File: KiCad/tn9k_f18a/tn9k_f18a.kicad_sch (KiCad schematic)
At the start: 9 parts, among them J1 Conn_01x20, J2 Conn_01x20, J3 Conn_01x24, J4 Conn_01x24, J5 Conn_02x04_Counter_Clockwise, J6 Conn_02x08_Odd_Even, U1 SN74LVC245, U2 SN74LVC245, U3 SN74LVC245

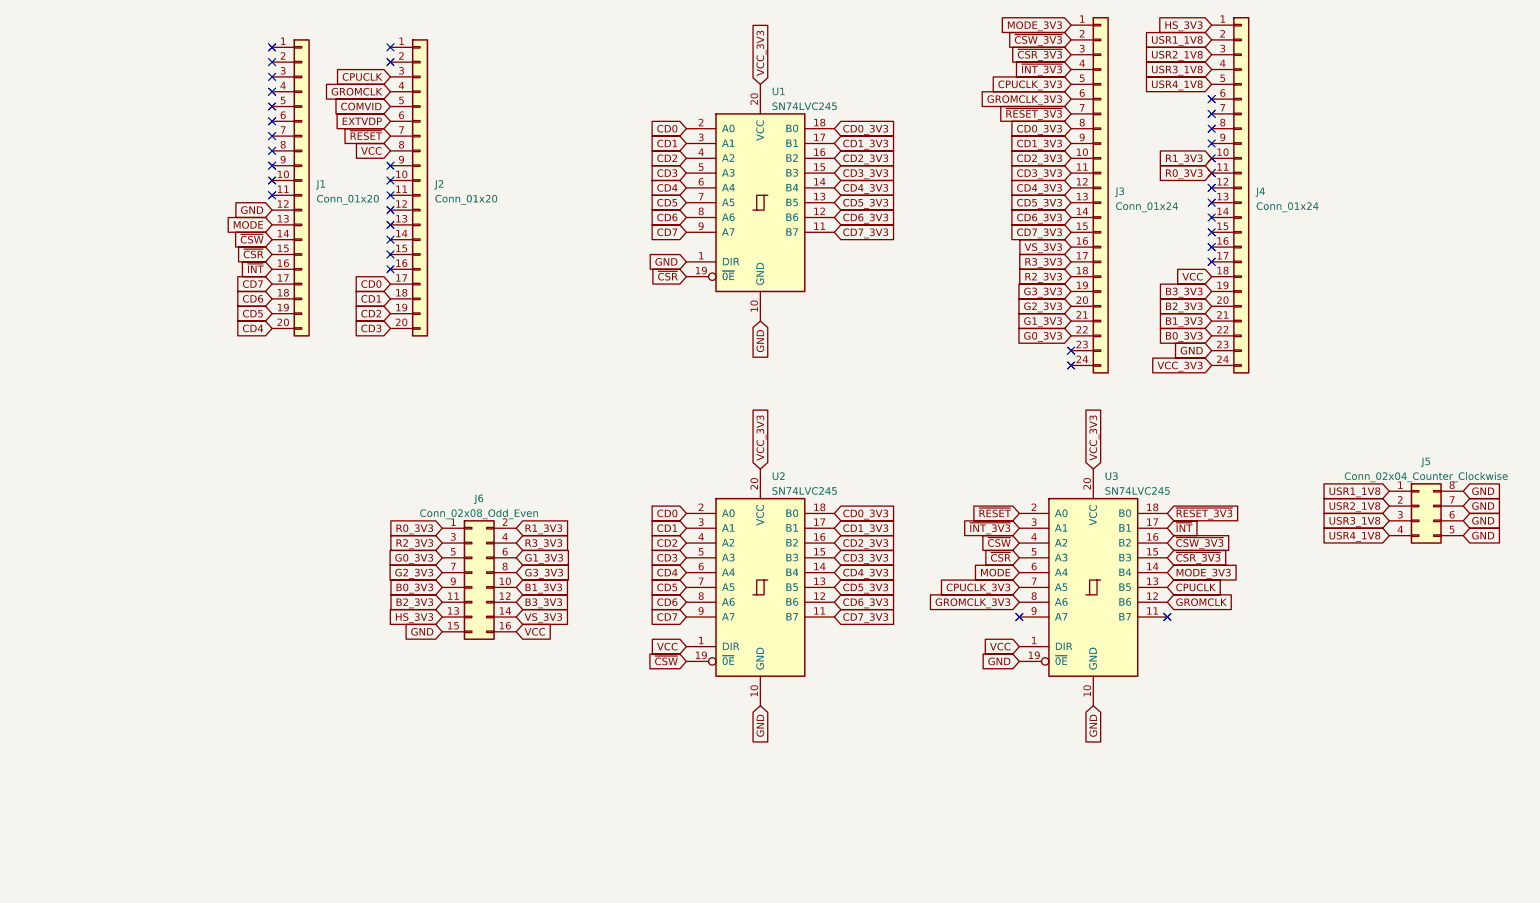
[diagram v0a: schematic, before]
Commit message: SMD version
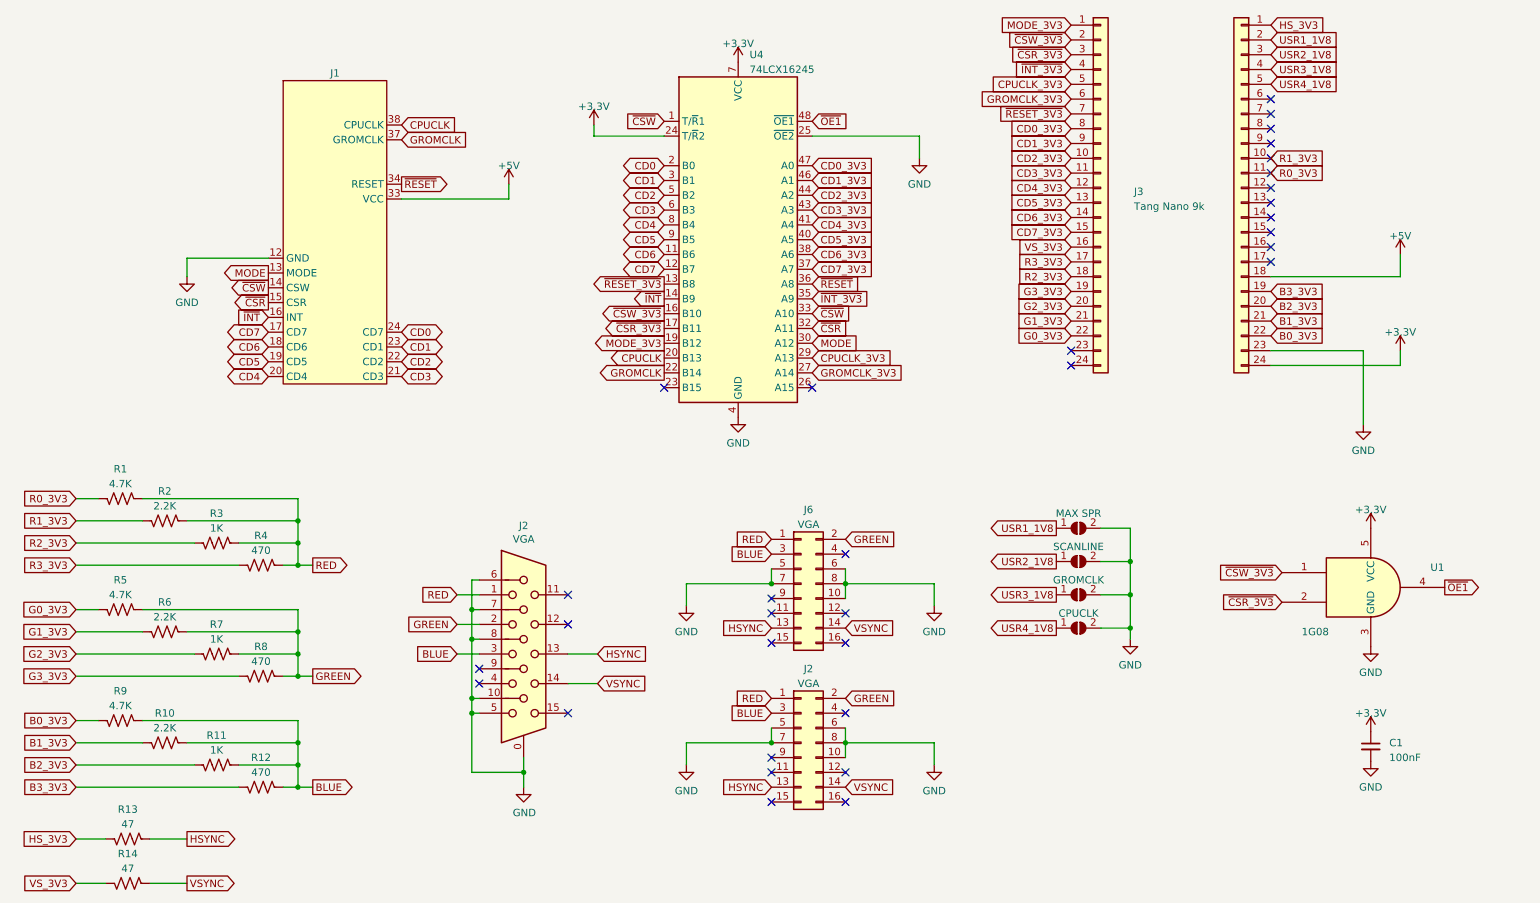
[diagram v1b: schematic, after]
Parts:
- removed J1, J2: Conn_01x20, Connector_PinHeader_2.54mm:PinHeader_1x20_P2.54mm_Vertical, symbol Connector_Generic:Conn_01x20
- removed J5: Conn_02x04_Counter_Clockwise, Button_Switch_THT:SW_DIP_SPSTx04_Slide_6.7x11.72mm_W7.62mm_P2.54mm_LowProfile, symbol Connector_Generic:Conn_02x04_Counter_Clockwise
- removed U1, U2, U3: SN74LVC245, Package_DIP:DIP-20_W7.62mm_Socket_LongPads, symbol tms9118a_sym:SN74LVC245
- added C1: 100nF, Capacitor_SMD:C_0603_1608Metric_Pad1.08x0.95mm_HandSolder, symbol Device:C_Small
- added J1: ~, f18a_footprints:TMS99xxA_Replacement, symbol f18a_tn9k:TMS99xxA_Replacement
- added J2: VGA, Connector_Dsub:DSUB-15-HD_Female_Horizontal_P2.29x1.98mm_EdgePinOffset3.03mm_Housed_MountingHolesOffset4.94mm, symbol Connector:DB15_Female_HighDensity_MountingHoles
- added J2: VGA, Connector_PinHeader_2.54mm:PinHeader_2x08_P2.54mm_Vertical, symbol Connector_Generic:Conn_02x08_Odd_Even
- added JP1: MAX SPR, Jumper:SolderJumper-2_P1.3mm_Open_RoundedPad1.0x1.5mm, symbol Jumper:SolderJumper_2_Open
- added JP2: SCANLINE, Jumper:SolderJumper-2_P1.3mm_Open_RoundedPad1.0x1.5mm, symbol Jumper:SolderJumper_2_Open
- added JP3: GROMCLK, Jumper:SolderJumper-2_P1.3mm_Open_RoundedPad1.0x1.5mm, symbol Jumper:SolderJumper_2_Open
- added JP4: CPUCLK, Jumper:SolderJumper-2_P1.3mm_Open_RoundedPad1.0x1.5mm, symbol Jumper:SolderJumper_2_Open
- added R1, R5, R9: 4.7K, Resistor_SMD:R_0603_1608Metric_Pad0.98x0.95mm_HandSolder, symbol Device:R_US
- added R10, R2, R6: 2.2K, Resistor_SMD:R_0603_1608Metric_Pad0.98x0.95mm_HandSolder, symbol Device:R_US
- added R11, R3, R7: 1K, Resistor_SMD:R_0603_1608Metric_Pad0.98x0.95mm_HandSolder, symbol Device:R_US
- added R12, R4, R8: 470, Resistor_SMD:R_0603_1608Metric_Pad0.98x0.95mm_HandSolder, symbol Device:R_US
- added R13, R14: 47, Resistor_SMD:R_0603_1608Metric_Pad0.98x0.95mm_HandSolder, symbol Device:R_US
- added U1: 1G08, Package_TO_SOT_SMD:SOT-23-5_HandSoldering, symbol 74xGxx:74AHC1G08
- added U4: 74LCX16245, Package_SO:TSSOP-48_6.1x12.5mm_P0.5mm, symbol 74xx:MC74LCX16245DT
- J3: value Conn_01x24 -> Tang Nano 9k
- J4: value Conn_01x24 -> TN9k/2
- J6: value Conn_02x08_Odd_Even -> VGA
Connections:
- net B0_3V3: now also R9.2; no longer J6.9 (Pin_9)
- net B1_3V3: now also R10.2; no longer J6.10 (Pin_10)
- net B2_3V3: now also R11.2; no longer J6.11 (Pin_11)
- net B3_3V3: now also R12.2; no longer J6.12 (Pin_12)
- net CD0: now also J1.24 (CD7), U4.2 (B0)
- net CD0_3V3: now also U4.47 (A0)
- net CD1: now also J1.23 (CD1), U4.3 (B1)
- net CD1_3V3: now also U4.46 (A1)
- net CD2: now also J1.22 (CD2), U4.5 (B2)
- net CD2_3V3: now also U4.44 (A2)
- net CD3: now also J1.21 (CD3), U4.6 (B3)
- net CD3_3V3: now also U4.43 (A3)
- net CD4: now also J1.20 (CD4), U4.8 (B4)
- net CD4_3V3: now also U4.41 (A4)
- net CD5: now also J1.19 (CD5), U4.9 (B5)
- net CD5_3V3: now also U4.40 (A5)
- net CD6: now also J1.18 (CD6), U4.11 (B6)
- net CD6_3V3: now also U4.38 (A6)
- net CD7: now also J1.17 (CD7), U4.12 (B7)
- net CD7_3V3: now also U4.37 (A7)
- net CPUCLK: now also J1.38 (CPUCLK), U4.20 (B13)
- net CPUCLK_3V3: now also U4.29 (A13)
- net G0_3V3: now also R5.2; no longer J6.5 (Pin_5)
- net G1_3V3: now also R6.2; no longer J6.6 (Pin_6)
- net G2_3V3: now also R7.2; no longer J6.7 (Pin_7)
- net G3_3V3: now also R8.2; no longer J6.8 (Pin_8)
- net GND: now also J6.10 (Pin_10), J6.5 (Pin_5), J6.6 (Pin_6), J6.7 (Pin_7), J6.8 (Pin_8), C1.2, J1.12 (GND), J2.0, J2.10, J2.10 (Pin_10), J2.5, J2.5 (Pin_5), J2.6, J2.6 (Pin_6), J2.7, J2.7 (Pin_7), J2.8, J2.8 (Pin_8), JP1.2 (B), JP2.2 (B), JP3.2 (B), JP4.2 (B), U1.3 (GND), U4.10 (GND), U4.15 (GND), U4.21 (GND), U4.25 (~{OE2}), U4.28 (GND), U4.34 (GND), U4.39 (GND), U4.4 (GND), U4.45 (GND); no longer J6.15 (Pin_15)
- net GROMCLK: now also J1.37 (GROMCLK), U4.22 (B14)
- net GROMCLK_3V3: now also U4.27 (A14)
- net HS_3V3: now also R13.2; no longer J6.13 (Pin_13)
- net MODE: now also J1.13 (MODE), U4.30 (A12)
- net MODE_3V3: now also U4.19 (B12)
- net R0_3V3: now also R1.2; no longer J6.1 (Pin_1)
- net R1_3V3: now also R2.2; no longer J6.2 (Pin_2)
- net R2_3V3: now also R3.2; no longer J6.3 (Pin_3)
- net R3_3V3: now also R4.2; no longer J6.4 (Pin_4)
- net USR1_1V8: now also JP1.1 (A)
- net USR2_1V8: now also JP2.1 (A)
- net USR3_1V8: now also JP3.1 (A)
- net USR4_1V8: now also JP4.1 (A)
- net VS_3V3: now also R14.2; no longer J6.14 (Pin_14)
- net ~{CSR_3V3}: now also U1.2, U4.17 (B11)
- net ~{CSR}: now also J1.15 (CSR), U4.32 (A11)
- net ~{CSW_3V3}: now also U1.1, U4.16 (B10)
- net ~{CSW}: now also J1.14 (CSW), U4.1 (T/~{R}1), U4.33 (A10)
- net ~{INT_3V3}: now also U4.35 (A9)
- net ~{INT}: now also J1.16 (INT), U4.14 (B9)
- net ~{RESET_3V3}: now also U4.13 (B8)
- net ~{RESET}: now also J1.34 (RESET), U4.36 (A8)
- net VCC: no longer names the net of J6.16 (Pin_16)
- net VCC: no longer J4.18 (Pin_18)
- net VCC_3V3 renamed +3.3V
- net +3.3V: now also C1.1, U1.5 (VCC), U4.18 (VCC), U4.24 (T/~{R}2), U4.31 (VCC), U4.42 (VCC), U4.7 (VCC)
- new net +5V: J1.33 (VCC), J4.18 (Pin_18)
- new net BLUE: J2.3, J2.3 (Pin_3), J6.3 (Pin_3), R10.1, R11.1, R12.1, R9.1
- new net GREEN: J2.2, J2.2 (Pin_2), J6.2 (Pin_2), R5.1, R6.1, R7.1, R8.1
- new net HSYNC: J2.13, J2.13 (Pin_13), J6.13 (Pin_13), R13.1
- new net RED: J2.1, J2.1 (Pin_1), J6.1 (Pin_1), R1.1, R2.1, R3.1, R4.1
- new net VSYNC: J2.14, J2.14 (Pin_14), J6.14 (Pin_14), R14.1
- new net ~{OE1}: U1.4, U4.48 (~{OE1})
- no-connect marks 37 -> 33
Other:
- moved on the sheet: J6
